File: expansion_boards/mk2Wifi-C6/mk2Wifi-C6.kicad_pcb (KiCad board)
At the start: 2 copper layers, 51 x 24.2 mm, 33 parts, among them J0 TRIG_EXT, J2 USB_C_Receptacle_USB2.0_16P, J3 UART_EXT, J4 OLED, SW1 SW_Push, U1 ESP32-C3-MINI-1, U2 AP2112K-3.3

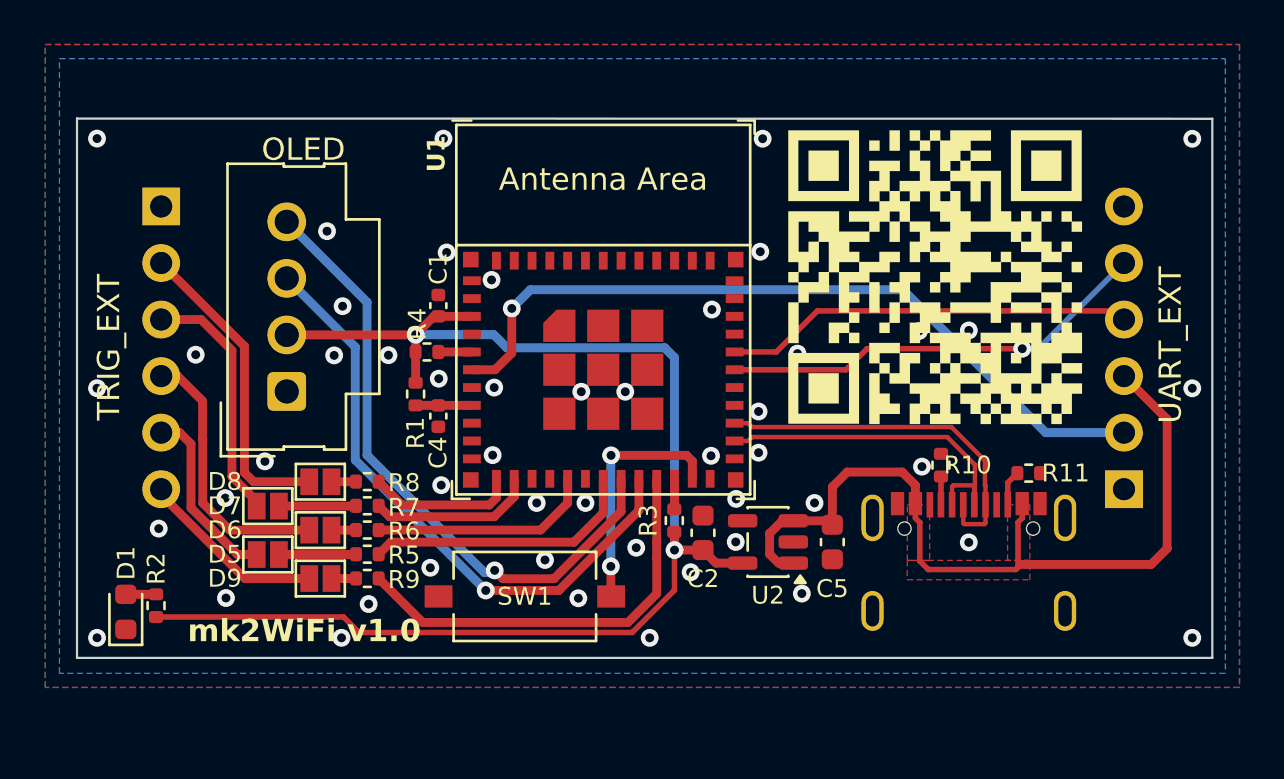
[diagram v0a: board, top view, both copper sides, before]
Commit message: Update mk2Wifi-C6 PCB layout, routing, and LCSC refs
- Complete PCB routing for ESP32-C6-MINI-1 board
- Add GND copper pours on F.Cu and B.Cu with 51 stitching vias
- Add +5V pour on F.Cu
- Add USB diff pair, I2C, UART, GPIO signal routing
- Add LCSC part number C5736265 for U1 (ESP32-C6-MINI-1-N4)
- Update project settings (USB net class, track widths)

Co-Authored-By: Claude Opus 4.6 <noreply@anthropic.com>
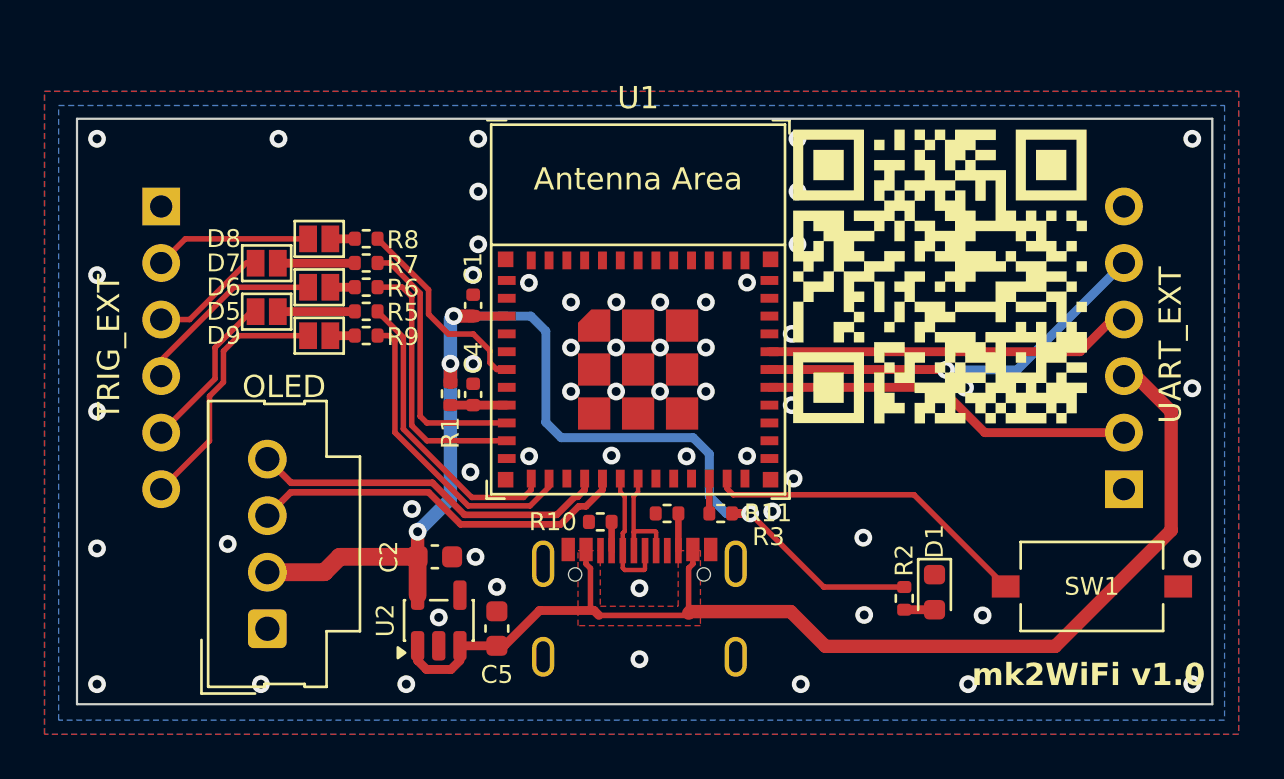
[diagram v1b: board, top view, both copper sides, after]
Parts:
- removed R4: 10K, Resistor_SMD:R_0402_1005Metric
- U1: value ESP32-C3-MINI-1 -> ESP32-C6-MINI-1/U; footprint PCM_Espressif:ESP32-C3-MINI-1 -> PCM_Espressif:ESP32-C6-MINI-1
- moved D1 36.3 mm to (89.1, 63.3), turned to -90 degrees
- moved R2 33.6 mm to (87.7, 63.5), turned to -90 degrees
- moved SW1 25.5 mm to (96.2, 63.0), turned to 180 degrees
- moved R11 16.3 mm to (77.1, 59.7), turned to 180 degrees
- moved C5 15.6 mm to (69.4, 64.9), turned to 90 degrees
- moved R10 15.5 mm to (74.1, 60.1), turned to 180 degrees
- moved U2 15.2 mm to (66.8, 64.5), turned to 90 degrees
- moved J2 14.9 mm to (76.1, 64.9)
- moved C2 12.1 mm to (66.7, 61.7), turned to 0 degrees
- moved JP4 10.9 mm to (59.1, 50.7)
- moved JP5 10.9 mm to (61.5, 51.7)
- moved R6 10.9 mm to (63.6, 49.6)
- moved R7 10.9 mm to (63.6, 48.5)
- moved JP1 10.9 mm to (61.5, 47.4)
- moved JP2 10.9 mm to (59.1, 48.5)
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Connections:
- R5 pad 2: Net-(U1-GPIO4/ADC1_CH4) -> Net-(U1-GPIO0/ADC1_CH0/XTAL_32K_P)
- R6 pad 1: Net-(U1-GPIO10) -> Net-(U1-MTDI/GPIO5/ADC1_CH5)
- R7 pad 1: Net-(U1-GPIO1/ADC1_CH1/XTAL_32K_N) -> Net-(U1-MTMS/GPIO4/ADC1_CH4)
- R8 pad 1: Net-(U1-GPIO0/ADC1_CH0/XTAL_32K_P) -> Net-(U1-GPIO3/ADC1_CH3)
- R9 pad 2: Net-(U1-GPIO7) -> Net-(U1-GPIO1/ADC1_CH1/XTAL_32K_N)
- U1 pad 10: unconnected-(U1-NC-Pad10) -> Net-(U1-MTDI/GPIO5/ADC1_CH5)
- U1 pad 15: unconnected-(U1-NC-Pad15) -> /SDA
- U1 pad 16: Net-(U1-GPIO10) -> /SCL
- U1 pad 17: unconnected-(U1-NC-Pad17) -> /USB_DN
- U1 pad 18: Net-(U1-GPIO4/ADC1_CH4) -> /USB_DP
- U1 pad 19: /SDA -> unconnected-(U1-GPIO14-Pad19)
- U1 pad 20: /SCL -> unconnected-(U1-GPIO15-Pad20)
- U1 pad 21: Net-(U1-GPIO7) -> unconnected-(U1-NC-Pad21)
- U1 pad 26: /USB_DN -> unconnected-(U1-GPIO20-Pad26)
- U1 pad 27: /USB_DP -> unconnected-(U1-GPIO21-Pad27)
- U1 pad 29: unconnected-(U1-NC-Pad29) -> /DS18B20
- U1 pad 5: /GPIO2 -> unconnected-(U1-GPIO2/ADC1_CH2-Pad5)
- U1 pad 6: /DS18B20 -> Net-(U1-GPIO3/ADC1_CH3)
- U1 pad 9: unconnected-(U1-NC-Pad9) -> Net-(U1-MTMS/GPIO4/ADC1_CH4)
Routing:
- net Net-(U1-GPIO7): track 19.0 -> 0.00 mm
- net /DS18B20: track 34.6 -> 16.8 mm, vias 1 -> 0
- net +5V: track 38.1 -> 54.3 mm
- net Net-(U1-GPIO4/ADC1_CH4): track 12.4 -> 0.00 mm
- net /SDA: track 28.5 -> 16.3 mm, vias 1 -> 0
- net Net-(U1-MTDI/GPIO5/ADC1_CH5): track 0.00 -> 12.1 mm
- net Net-(U1-MTMS/GPIO4/ADC1_CH4): track 0.00 -> 12.0 mm
- net /USB_DP: track 16.6 -> 5.98 mm
- net /SCL: track 27.5 -> 17.2 mm, vias 1 -> 0
- net Net-(U1-GPIO10): track 10.1 -> 0.00 mm
- net /USB_DN: track 15.9 -> 6.01 mm
- net Net-(U1-GPIO3/ADC1_CH3): track 0.00 -> 9.20 mm
- net +3V3: track 61.5 -> 53.1 mm, vias 2 -> 4
- net Net-(J0-Pin_2): track 14.0 -> 7.05 mm
- net Net-(U1-GPIO0/ADC1_CH0/XTAL_32K_P): track 6.71 -> 13.4 mm
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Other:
- board size 51 x 24.2 mm -> 51 x 26.3 mm
